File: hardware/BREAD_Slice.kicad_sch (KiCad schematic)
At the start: 15 parts, among them J1 I2C_01x04, J2 Conn_01x10_Female

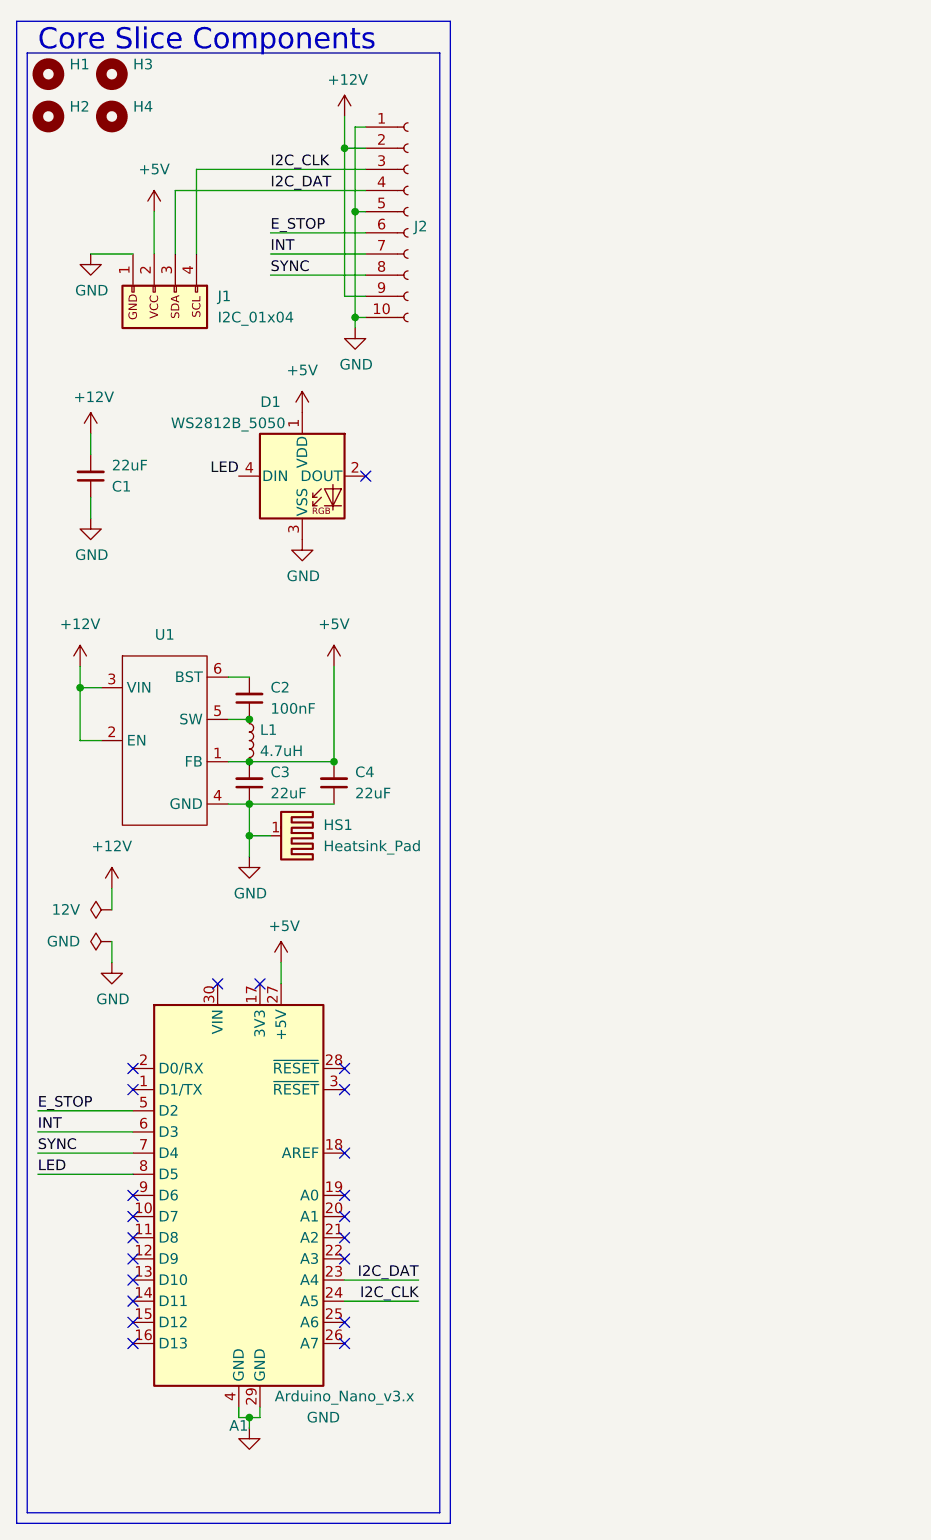
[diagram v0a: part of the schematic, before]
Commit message: updated template and added pcb vars for prototyping
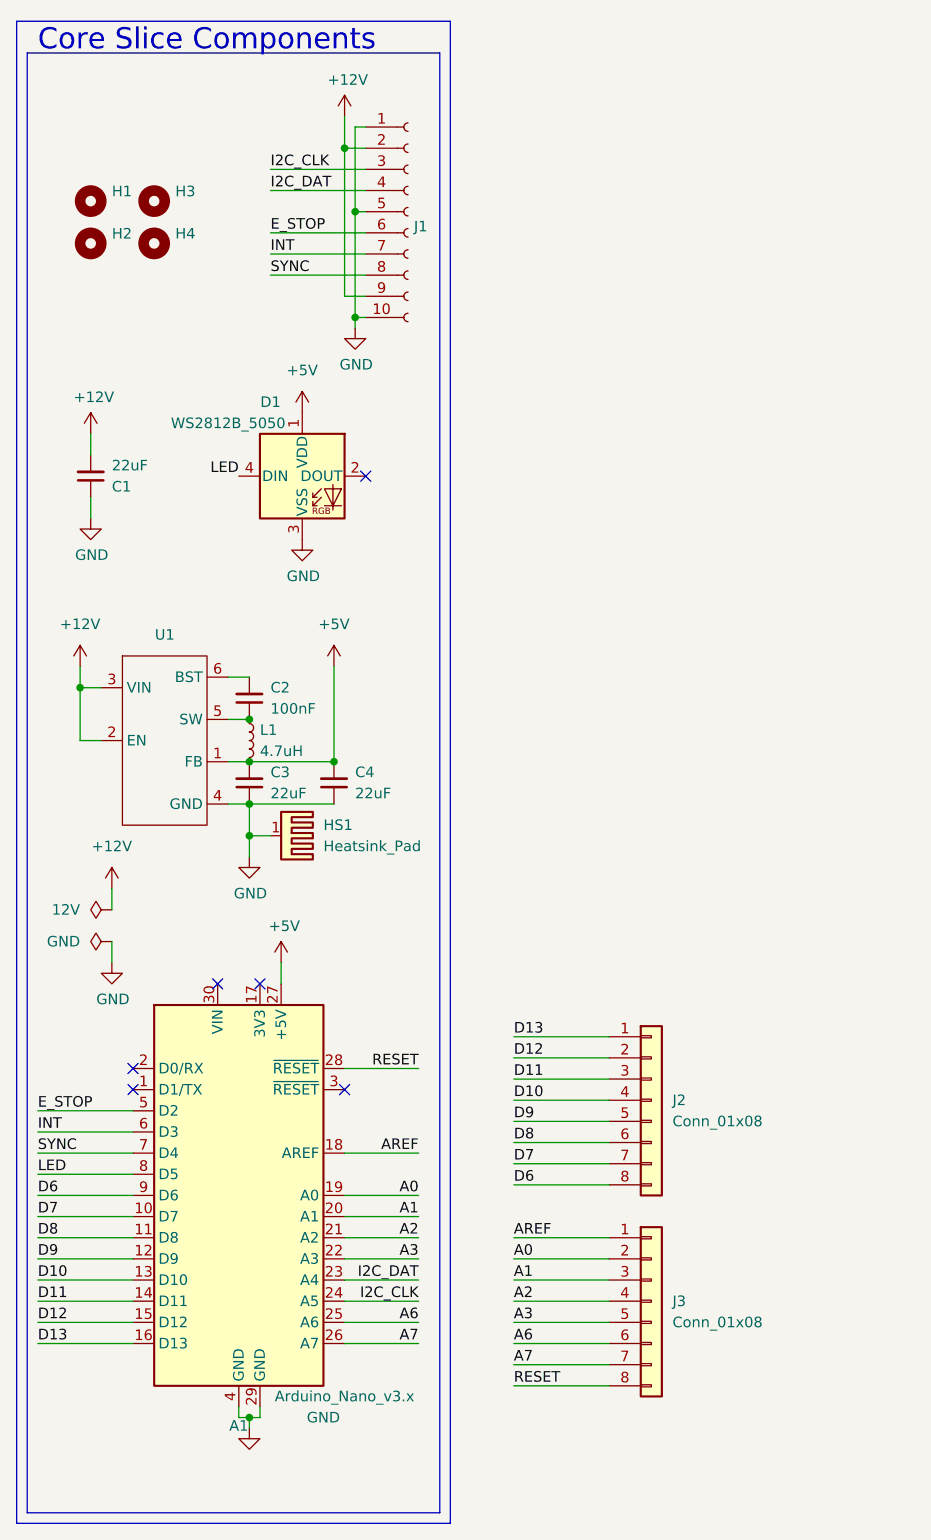
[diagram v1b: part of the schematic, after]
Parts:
- removed J1: I2C_01x04, Connector_JST:JST_SH_SM04B-SRSS-TB_1x04-1MP_P1.00mm_Horizontal, symbol SparkFun-Connector:I2C_01x04
- added J2, J3: Conn_01x08, TerminalBlock_4Ucon:TerminalBlock_4Ucon_1x08_P3.50mm_Horizontal, symbol Connector_Generic:Conn_01x08
- renumbered J2 to J1
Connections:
- net D7: now reaches A1.10 (D7)
- net D7: now also J2.7 (Pin_7)
- net D8: now reaches A1.11 (D8)
- net D8: now also J2.6 (Pin_6)
- net D9: now reaches A1.12 (D9)
- net D9: now also J2.5 (Pin_5)
- net D10: now reaches A1.13 (D10)
- net D10: now also J2.4 (Pin_4)
- net D11: now reaches A1.14 (D11)
- net D11: now also J2.3 (Pin_3)
- net D12: now reaches A1.15 (D12)
- net D12: now also J2.2 (Pin_2)
- net D13: now reaches A1.16 (D13)
- net D13: now also J2.1 (Pin_1)
- net AREF: now reaches A1.18 (AREF)
- net AREF: now also J3.1 (Pin_1)
- net A0: now reaches A1.19 (A0)
- net A0: now also J3.2 (Pin_2)
- net A1: now reaches A1.20 (A1)
- net A1: now also J3.3 (Pin_3)
- net A2: now reaches A1.21 (A2)
- net A2: now also J3.4 (Pin_4)
- net A3: now reaches A1.22 (A3)
- net A3: now also J3.5 (Pin_5)
- net A6: now reaches A1.25 (A6)
- net A6: now also J3.6 (Pin_6)
- net A7: now reaches A1.26 (A7)
- net A7: now also J3.7 (Pin_7)
- net RESET: now reaches A1.28 (~{RESET})
- net RESET: now also J3.8 (Pin_8)
- net D6: now reaches A1.9 (D6)
- net D6: now also J2.8 (Pin_8)
- no-connect marks 22 -> 6
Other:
- moved on the sheet: H1, H2, H3, H4
